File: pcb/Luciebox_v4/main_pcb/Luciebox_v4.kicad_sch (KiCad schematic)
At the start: 64 parts, among them J1 USB_B_Mini, J2 USB_B_Mini, Q1 P-Channel MOSFET, Q2 NPN transistor, T1 terminal_8x1, T2 terminal_3x1, T4 terminal_8x1, T5 terminal_3x1, T6 terminal_8x1, T7 terminal_8x1, T8 terminal_8x1, U1 CA56-12SRWA, U2 8X8PADS, U3 ATmega328-PU, Y1 16MHz

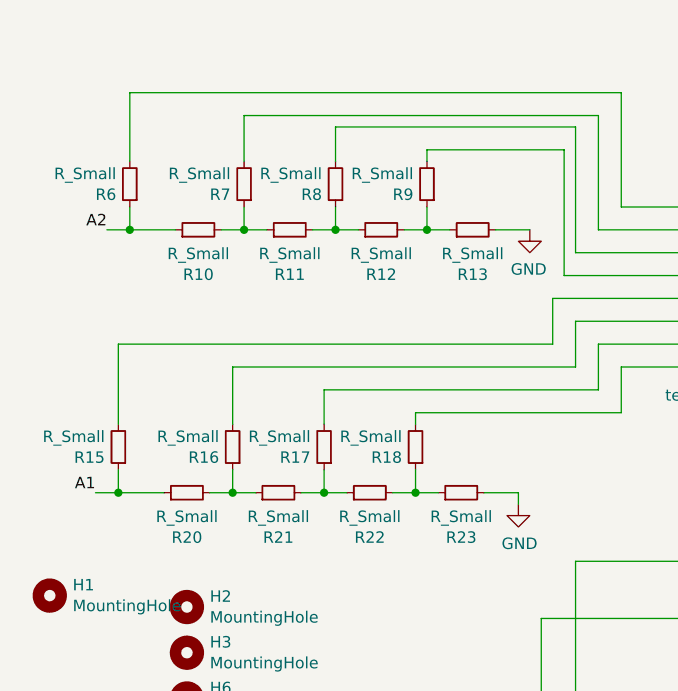
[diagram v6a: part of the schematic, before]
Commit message: Main pcb v4 values
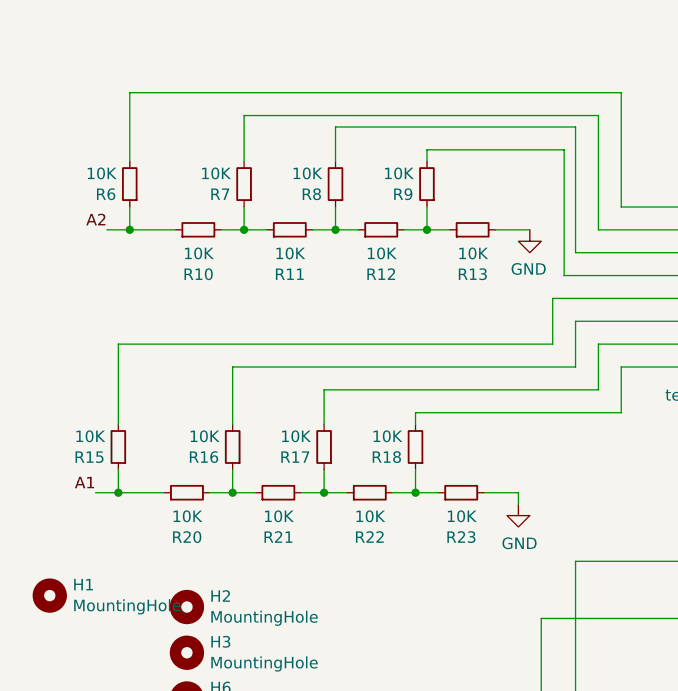
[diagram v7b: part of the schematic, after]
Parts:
- R10, R11, R12, R13, R15, R16, R17, R18, R20, R21, R22, R23, R6, R7, R8, R9: value R_Small -> 10K
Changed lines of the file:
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@@
       (effects (font (size 1.27 1.27)) (justify left))
     )
-    (property "Value" "R_Small" (id 1) (at 46.7614 113.157 0)
+    (property "Value" "10K" (id 1) (at 46.7614 113.157 0)
       (effects (font (size 1.27 1.27)) (justify left))
     )
@@
       (effects (font (size 1.27 1.27)) (justify left))
     )
-    (property "Value" "R_Small" (id 1) (at 58.1914 83.947 0)
+    (property "Value" "10K" (id 1) (at 58.1914 83.947 0)
       (effects (font (size 1.27 1.27)) (justify left))
     )
@@
     (in_bom yes) (on_board yes)
     (property "Reference" "R22" (id 0) (at 53.34 124.3584 90))
-    (property "Value" "R_Small" (id 1) (at 53.34 122.047 90))
+    (property "Value" "10K" (id 1) (at 53.34 122.047 90))
     (property "Footprint" "Luciebox:0603_1608Metric" (id 2) (at 53.34 119.38 0)
       (effects (font (size 1.27 1.27)) hide)
@@
       (effects (font (size 1.27 1.27)) (justify left))
     )
-    (property "Value" "R_Small" (id 1) (at 48.0314 83.947 0)
+    (property "Value" "10K" (id 1) (at 48.0314 83.947 0)
       (effects (font (size 1.27 1.27)) (justify left))
     )
@@
     (in_bom yes) (on_board yes)
     (property "Reference" "R13" (id 0) (at 64.77 95.1484 90))
-    (property "Value" "R_Small" (id 1) (at 64.77 92.837 90))
+    (property "Value" "10K" (id 1) (at 64.77 92.837 90))
     (property "Footprint" "Luciebox:0603_1608Metric" (id 2) (at 64.77 90.17 0)
       (effects (font (size 1.27 1.27)) hide)
@@
     (in_bom yes) (on_board yes)
     (property "Reference" "R21" (id 0) (at 43.18 124.3584 90))
-    (property "Value" "R_Small" (id 1) (at 43.18 122.047 90))
+    (property "Value" "10K" (id 1) (at 43.18 122.047 90))
     (property "Footprint" "Luciebox:0603_1608Metric" (id 2) (at 43.18 119.38 0)
       (effects (font (size 1.27 1.27)) hide)
@@
     (in_bom yes) (on_board yes)
     (property "Reference" "R10" (id 0) (at 34.29 95.1484 90))
-    (property "Value" "R_Small" (id 1) (at 34.29 92.837 90))
+    (property "Value" "10K" (id 1) (at 34.29 92.837 90))
     (property "Footprint" "Luciebox:0603_1608Metric" (id 2) (at 34.29 90.17 0)
       (effects (font (size 1.27 1.27)) hide)
@@
     (in_bom yes) (on_board yes)
     (property "Reference" "R23" (id 0) (at 63.5 124.3584 90))
-    (property "Value" "R_Small" (id 1) (at 63.5 122.047 90))
+    (property "Value" "10K" (id 1) (at 63.5 122.047 90))
     (property "Footprint" "Luciebox:0603_1608Metric" (id 2) (at 63.5 119.38 0)
       (effects (font (size 1.27 1.27)) hide)
@@
     (in_bom yes) (on_board yes)
     (property "Reference" "R12" (id 0) (at 54.61 95.1484 90))
-    (property "Value" "R_Small" (id 1) (at 54.61 92.837 90))
+    (property "Value" "10K" (id 1) (at 54.61 92.837 90))
     (property "Footprint" "Luciebox:0603_1608Metric" (id 2) (at 54.61 90.17 0)
       (effects (font (size 1.27 1.27)) hide)
@@
       (effects (font (size 1.27 1.27)) (justify left))
     )
-    (property "Value" "R_Small" (id 1) (at 56.9214 113.157 0)
+    (property "Value" "10K" (id 1) (at 56.9214 113.157 0)
       (effects (font (size 1.27 1.27)) (justify left))
     )
@@
       (effects (font (size 1.27 1.27)) (justify left))
     )
-    (property "Value" "R_Small" (id 1) (at 37.8714 83.947 0)
+    (property "Value" "10K" (id 1) (at 37.8714 83.947 0)
       (effects (font (size 1.27 1.27)) (justify left))
     )
@@
       (effects (font (size 1.27 1.27)) (justify left))
     )
-    (property "Value" "R_Small" (id 1) (at 36.6014 113.157 0)
+    (property "Value" "10K" (id 1) (at 36.6014 113.157 0)
       (effects (font (size 1.27 1.27)) (justify left))
     )
@@
       (effects (font (size 1.27 1.27)) (justify left))
     )
-    (property "Value" "R_Small" (id 1) (at 25.1714 83.947 0)
+    (property "Value" "10K" (id 1) (at 25.1714 83.947 0)
       (effects (font (size 1.27 1.27)) (justify left))
     )
@@
     (in_bom yes) (on_board yes)
     (property "Reference" "R20" (id 0) (at 33.02 124.3584 90))
-    (property "Value" "R_Small" (id 1) (at 33.02 122.047 90))
+    (property "Value" "10K" (id 1) (at 33.02 122.047 90))
     (property "Footprint" "Luciebox:0603_1608Metric" (id 2) (at 33.02 119.38 0)
       (effects (font (size 1.27 1.27)) hide)
@@
     (in_bom yes) (on_board yes)
     (property "Reference" "R11" (id 0) (at 44.45 95.1484 90))
-    (property "Value" "R_Small" (id 1) (at 44.45 92.837 90))
+    (property "Value" "10K" (id 1) (at 44.45 92.837 90))
     (property "Footprint" "Luciebox:0603_1608Metric" (id 2) (at 44.45 90.17 0)
       (effects (font (size 1.27 1.27)) hide)
@@
       (effects (font (size 1.27 1.27)) (justify left))
     )
-    (property "Value" "R_Small" (id 1) (at 23.9014 113.157 0)
+    (property "Value" "10K" (id 1) (at 23.9014 113.157 0)
       (effects (font (size 1.27 1.27)) (justify left))
     )
@@
     )
     (path "/ba907e0d-2755-4208-ab9b-bc3b980814be"
-      (reference "R6") (unit 1) (value "R_Small") (footprint "Luciebox:0603_1608Metric")
+      (reference "R6") (unit 1) (value "10K") (footprint "Luciebox:0603_1608Metric")
     )
     (path "/a5caf9f6-e03e-450e-bccc-1a8c713e9865"
-      (reference "R7") (unit 1) (value "R_Small") (footprint "Luciebox:0603_1608Metric")
+      (reference "R7") (unit 1) (value "10K") (footprint "Luciebox:0603_1608Metric")
     )
     (path "/57e345a7-fd4d-4640-953c-1489199ff73d"
-      (reference "R8") (unit 1) (value "R_Small") (footprint "Luciebox:0603_1608Metric")
+      (reference "R8") (unit 1) (value "10K") (footprint "Luciebox:0603_1608Metric")
     )
     (path "/4fab0b58-ef30-42ef-ad7e-ac6fcde0c659"
-      (reference "R9") (unit 1) (value "R_Small") (footprint "Luciebox:0603_1608Metric")
+      (reference "R9") (unit 1) (value "10K") (footprint "Luciebox:0603_1608Metric")
     )
     (path "/86e70297-1921-4ad8-afa6-10ea3d91a5e2"
-      (reference "R10") (unit 1) (value "R_Small") (footprint "Luciebox:0603_1608Metric")
+      (reference "R10") (unit 1) (value "10K") (footprint "Luciebox:0603_1608Metric")
     )
     (path "/cafac398-fa5d-421c-a165-c22160b2656a"
-      (reference "R11") (unit 1) (value "R_Small") (footprint "Luciebox:0603_1608Metric")
+      (reference "R11") (unit 1) (value "10K") (footprint "Luciebox:0603_1608Metric")
     )
     (path "/98e326ed-e2cf-4ade-b990-18608d81e1b1"
-      (reference "R12") (unit 1) (value "R_Small") (footprint "Luciebox:0603_1608Metric")
+      (reference "R12") (unit 1) (value "10K") (footprint "Luciebox:0603_1608Metric")
     )
     (path "/74027727-b456-4af2-bac7-7657954b8685"
-      (reference "R13") (unit 1) (value "R_Small") (footprint "Luciebox:0603_1608Metric")
+      (reference "R13") (unit 1) (value "10K") (footprint "Luciebox:0603_1608Metric")
     )
     (path "/ce0e7b73-afe8-49e1-bc6d-da3afc3850ae"
-      (reference "R15") (unit 1) (value "R_Small") (footprint "Luciebox:0603_1608Metric")
+      (reference "R15") (unit 1) (value "10K") (footprint "Luciebox:0603_1608Metric")
     )
     (path "/b27bb8f5-456f-4aba-8556-a2f3e3fb4705"
-      (reference "R16") (unit 1) (value "R_Small") (footprint "Luciebox:0603_1608Metric")
+      (reference "R16") (unit 1) (value "10K") (footprint "Luciebox:0603_1608Metric")
     )
     (path "/4a72747e-16aa-42f3-bf34-c035f4f7b4db"
-      (reference "R17") (unit 1) (value "R_Small") (footprint "Luciebox:0603_1608Metric")
+      (reference "R17") (unit 1) (value "10K") (footprint "Luciebox:0603_1608Metric")
     )
     (path "/9ff3d8ce-e8bc-46df-9c01-5053e905e02f"
-      (reference "R18") (unit 1) (value "R_Small") (footprint "Luciebox:0603_1608Metric")
+      (reference "R18") (unit 1) (value "10K") (footprint "Luciebox:0603_1608Metric")
     )
     (path "/5e50add6-1ac0-4932-806b-fcf7abcf36e0"
@@
     )
     (path "/be20703b-1e59-4c78-b4ab-5c4a215643c7"
-      (reference "R20") (unit 1) (value "R_Small") (footprint "Luciebox:0603_1608Metric")
+      (reference "R20") (unit 1) (value "10K") (footprint "Luciebox:0603_1608Metric")
     )
     (path "/7b4dd050-c1d9-49c8-9c0c-41e7a6459410"
-      (reference "R21") (unit 1) (value "R_Small") (footprint "Luciebox:0603_1608Metric")
+      (reference "R21") (unit 1) (value "10K") (footprint "Luciebox:0603_1608Metric")
     )
     (path "/562ca749-0a8d-4a2a-a3dd-59221c4ac0e6"
-      (reference "R22") (unit 1) (value "R_Small") (footprint "Luciebox:0603_1608Metric")
+      (reference "R22") (unit 1) (value "10K") (footprint "Luciebox:0603_1608Metric")
     )
     (path "/8aa802dc-26d5-4775-b483-19b41c28fd3e"
-      (reference "R23") (unit 1) (value "R_Small") (footprint "Luciebox:0603_1608Metric")
+      (reference "R23") (unit 1) (value "10K") (footprint "Luciebox:0603_1608Metric")
     )
     (path "/8d8d9b06-7e57-461a-bc65-1284b00714d2"
